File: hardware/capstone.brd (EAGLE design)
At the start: 160 x 100 mm, 30 parts, among them J1 61300311121, J2 61300311121, U1 BMP388, U2 LSM9DS1TR, U3 RFM95W-915S2

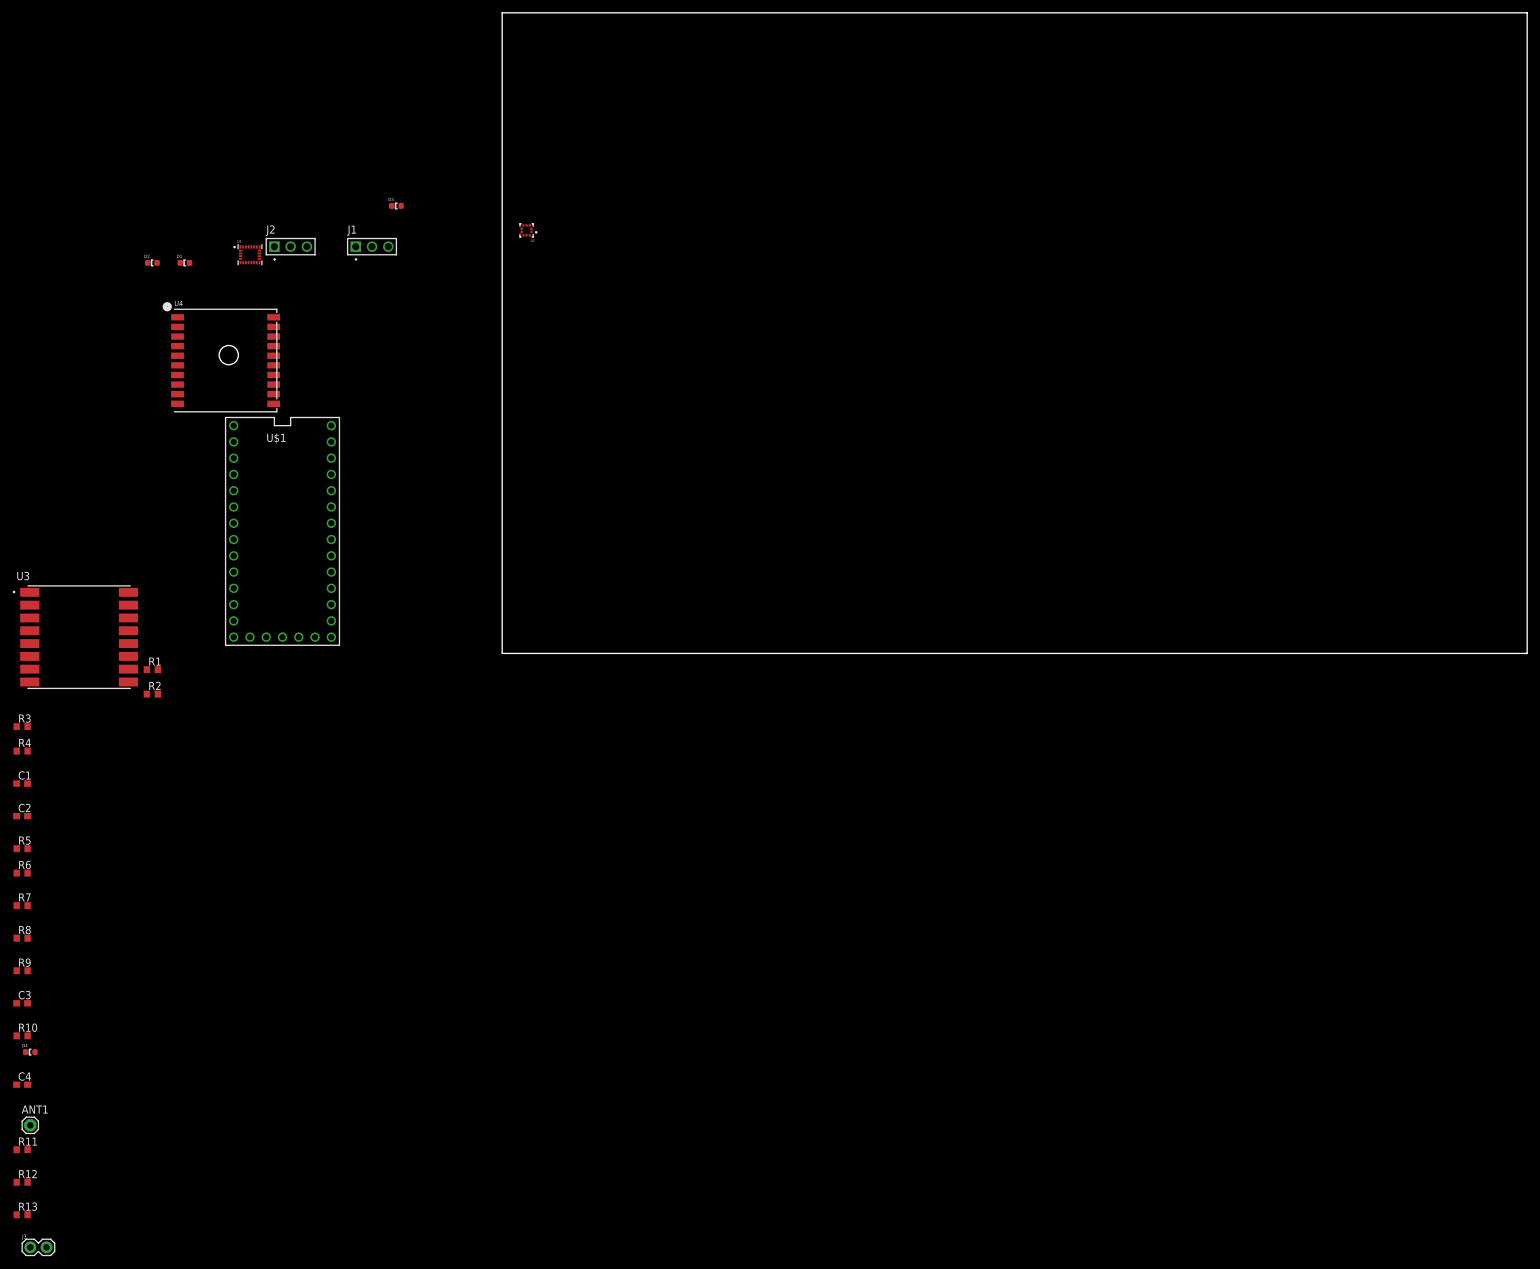
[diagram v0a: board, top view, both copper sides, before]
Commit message: Finished board routing
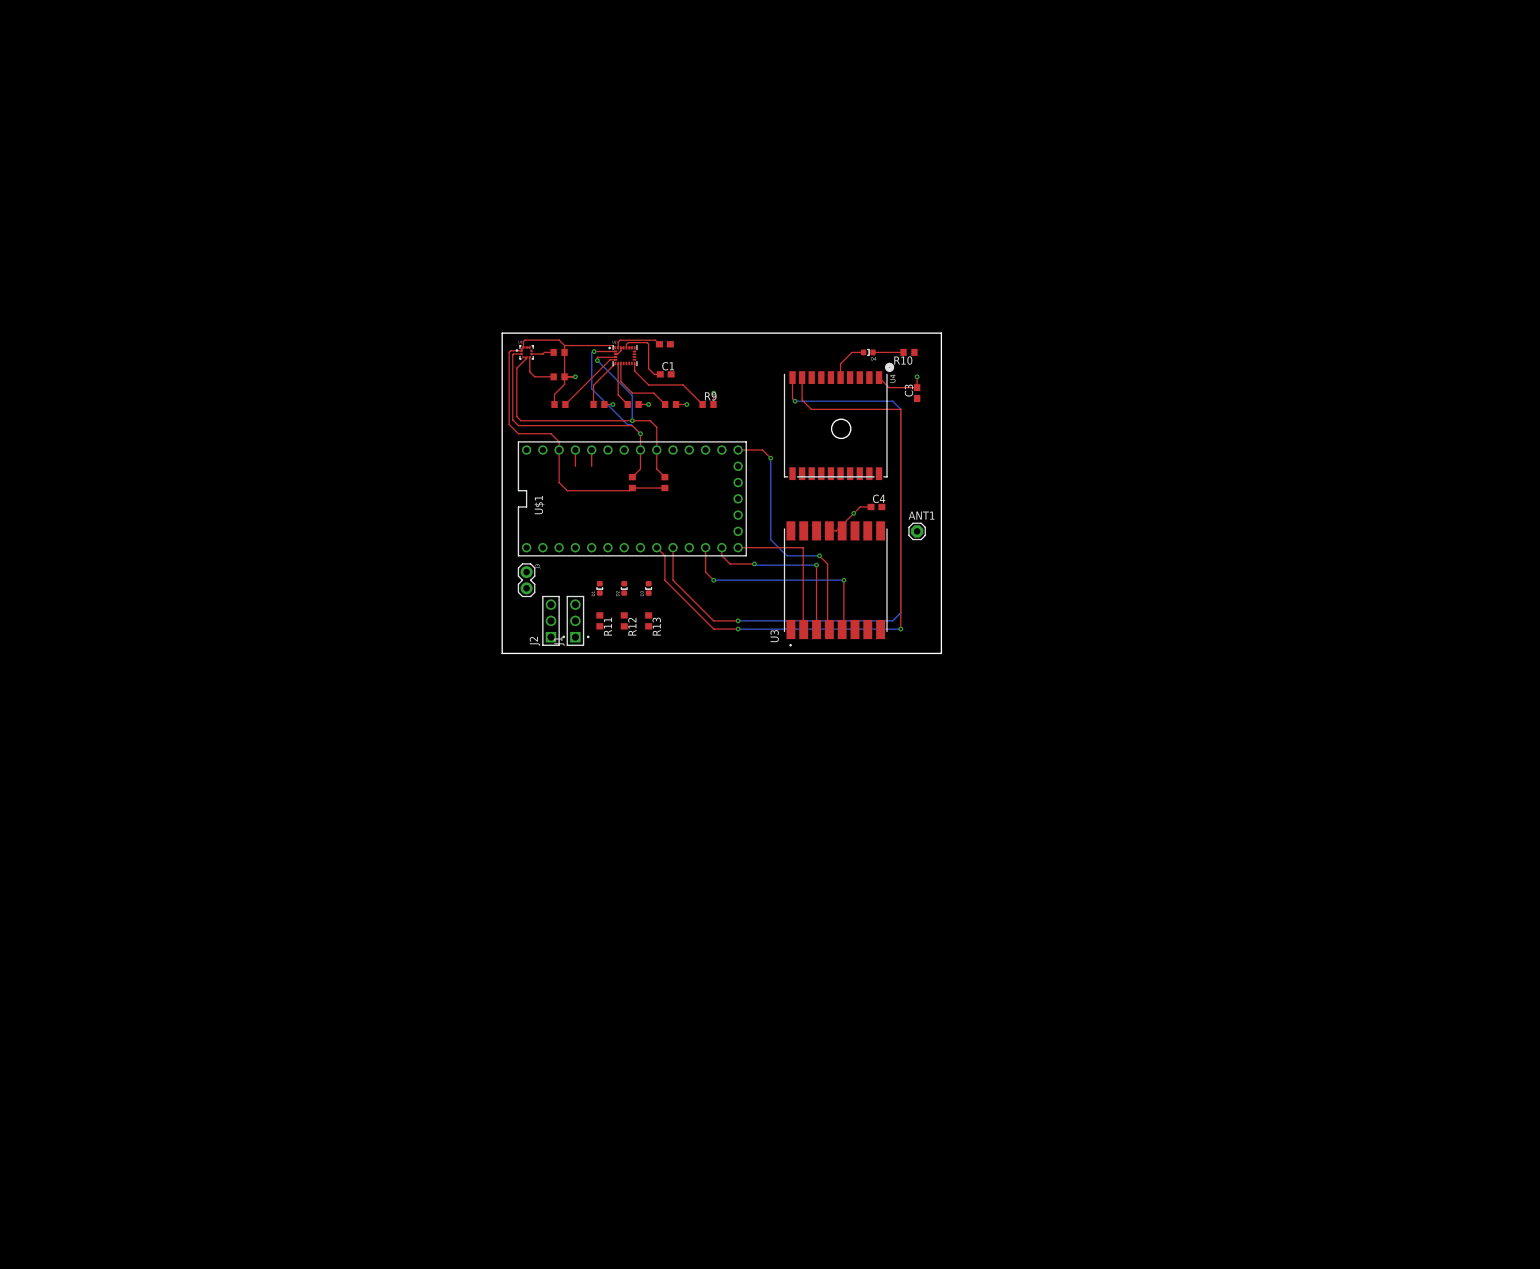
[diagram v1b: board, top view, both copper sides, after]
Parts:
- moved R10 174.8 mm to (63.5, 47.0), turned to 180 degrees
- moved D4 170.4 mm to (57.1, 47.0), turned to 180 degrees
- moved C3 169.1 mm to (64.8, 40.6), turned to 90 degrees
- moved ANT1 166.6 mm to (64.8, 19.1)
- moved C4 161.0 mm to (58.4, 22.9)
- moved R9 138.8 mm to (32.1, 38.9)
- moved R13 134.8 mm to (22.9, 5.08), turned to 270 degrees
- moved R8 131.1 mm to (26.3, 38.9)
- moved J3 130.8 mm to (3.81, 12.7), turned to 270 degrees
- moved R12 128.5 mm to (19.1, 5.08), turned to 270 degrees
- moved C2 124.5 mm to (25.4, 48.3)
- moved R7 123.4 mm to (20.4, 38.9)
- moved R11 122.3 mm to (15.2, 5.08), turned to 270 degrees
- moved C1 119.0 mm to (25.5, 43.6)
- moved U3 118.4 mm to (52.1, 11.4), turned to 90 degrees
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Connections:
- net GPS_RX: now also U$1.8
- net GPS_TX: now also U$1.7
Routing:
- net +3V3: track 0.00 -> 100.2 mm, vias 0 -> 7
- net GPS_TX: track 0.00 -> 99.4 mm, vias 0 -> 2
- net GPS_RX: track 0.00 -> 96.4 mm, vias 0 -> 2
- net SCL: track 0.00 -> 59.7 mm, vias 0 -> 2
- net SDA: track 0.00 -> 55.8 mm, vias 0 -> 2
- net SCK: track 0.00 -> 39.1 mm, vias 0 -> 2
- net GPS_CS: track 0.00 -> 33.9 mm, vias 0 -> 2
- net MOSI: track 0.00 -> 26.8 mm, vias 0 -> 2
- net MISO: track 0.00 -> 23.0 mm
- net LSM_DEN_AG: track 0.00 -> 13.9 mm
- net LSM_CS_M: track 0.00 -> 11.2 mm
- net LSM_SDO_AG: track 0.00 -> 10.7 mm
- net N$1: track 0.00 -> 10.2 mm
- net LSM_SDO_M: track 0.00 -> 7.81 mm
- net N$2: track 0.00 -> 7.72 mm
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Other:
- board size 160 x 100 mm -> 68.6 x 50 mm

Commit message: Finalize board
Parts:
- moved ANT1 1.80 mm to (63.5, 17.8)
- moved C4 0.89 mm to (58.4, 23.7)
- renumbered D1 to PWR_LED, D4 to FIX_LED
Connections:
- removed net ANT1: ANT1.1, U3.9
- net GND: now also ANT1.1, U3.9
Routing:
- net GND: track 0.93 -> 167.8 mm, vias 0 -> 9
- net +3V3: track 100.2 -> 211.0 mm, vias 7 -> 8
- net VIN: track 0.00 -> 37.1 mm
- net SERVO2: track 2.54 -> 25.7 mm, vias 0 -> 2
- net SERVO1: track 2.54 -> 25.2 mm, vias 0 -> 2
- net LED2: track 0.00 -> 6.14 mm
- net LED1: track 0.00 -> 5.62 mm
- net SCL: track 59.7 -> 64.8 mm
- net GPS_RX: track 96.4 -> 101.1 mm
- net SDA: track 55.8 -> 60.1 mm
- net GPS_TX: track 99.4 -> 103.3 mm
- net N$7: track 0.00 -> 3.50 mm
- net N$6: track 0.00 -> 3.50 mm
- net N$5: track 0.00 -> 3.50 mm
- net N$2: track 7.72 -> 9.70 mm
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- added copper zone on layer 16, net +3V3
- added copper zone on layer 1, net GND
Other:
- board size 68.6 x 50 mm -> 68.6 x 51.3 mm
- board text added: "GND"
- board text added: "SERVO"
